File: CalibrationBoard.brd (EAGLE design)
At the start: 100 x 80 mm, 113 parts, among them J1 BANANA_CONN, J2 BANANA_CONN, J3 BANANA_CONN, J4 BANANA_CONN, J5 BANANA_CONN, J6 BANANA_CONN, J7 BANANA_CONN, J8 BANANA_CONN, J9 BANANA_CONN, Q1 IRF540, U1 MAX6126AASA25+, U2 MAX6126AASA25+, U3 MAX6126AASA50+

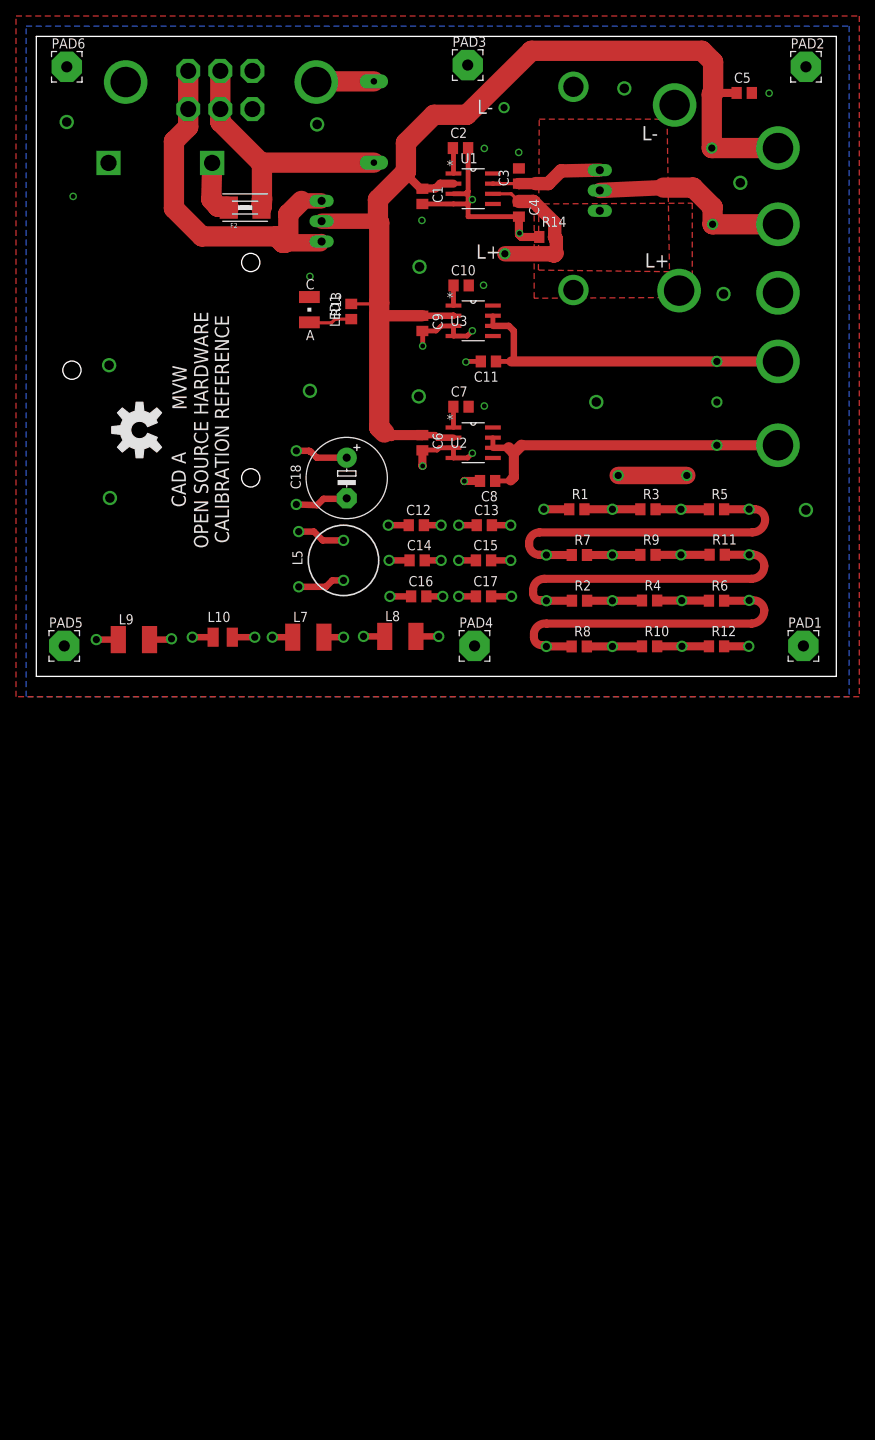
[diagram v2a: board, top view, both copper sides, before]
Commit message: Updates before PCB release to Fabrication
Updates before PCB release to Fabrication.
Component part numbers for purchase still need specifying.
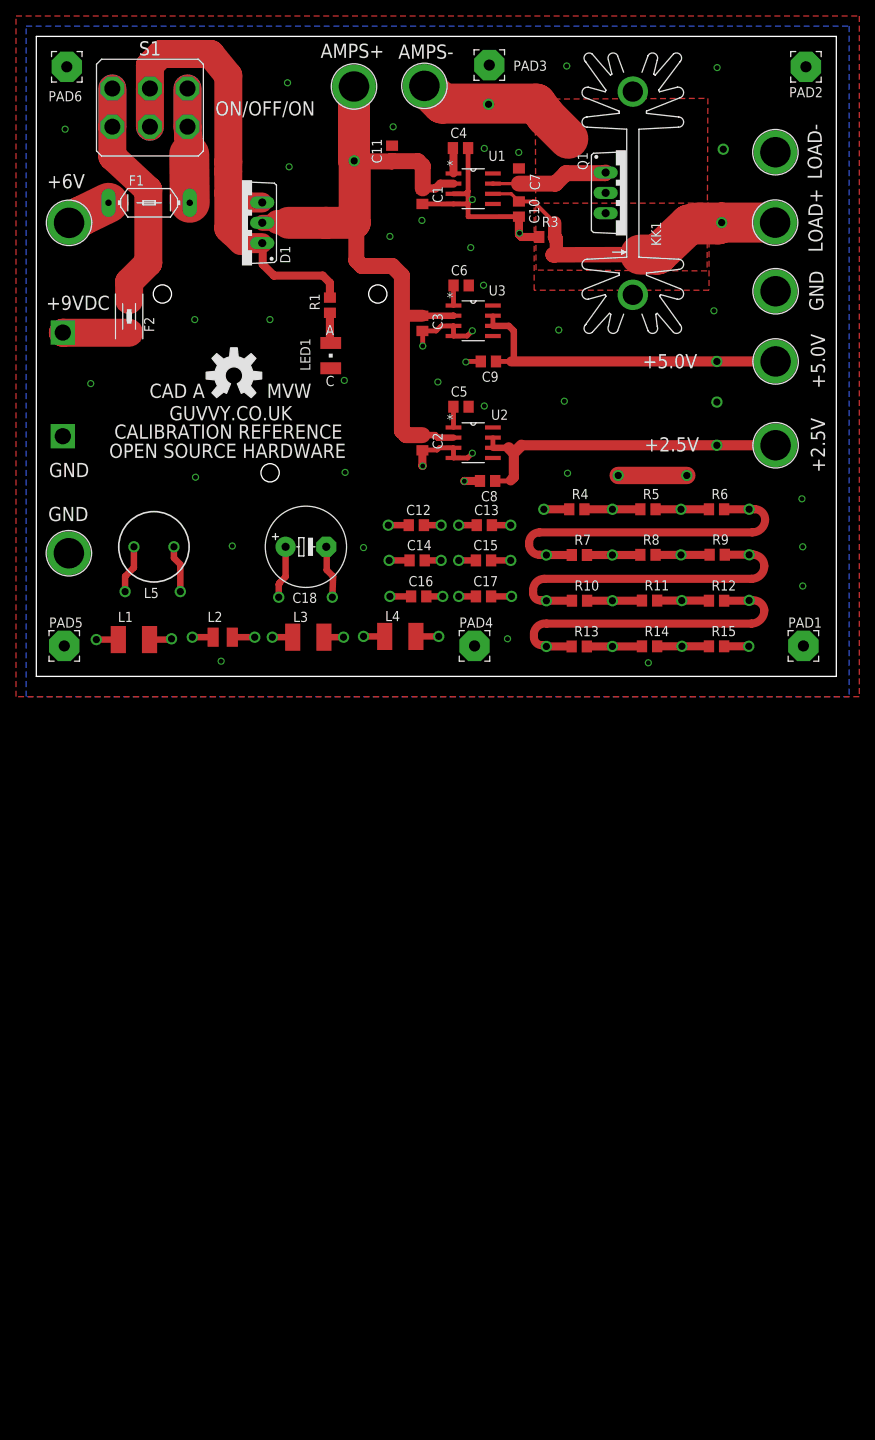
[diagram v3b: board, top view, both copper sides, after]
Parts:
- removed KK2: SK104-PAD, heatsink:SK104-PAD
- removed R2: 1k, rcl:R0805
- removed S3: 6A TOGGLE, switch:320-938
- removed TP51: TP_1MM_TH", TP_1MM_TH:TP_1MM_TH
- added KK1: SK104-PAD, heatsink:SK104-PAD
- added R15: 10Meg, rcl:R0805
- added S1: 5649A, Switch_320-938_Corrected:320-938
- added TP40: TP_1MM_TH", TP_1MM_TH:TP_1MM_TH
- C17: value 100uF -> 10uF
- C18: value (none) -> 100uF
- C2, C7: value 1uF -> 2.2uF
- C5, C6: value 2.2uF -> 1uF
- D1: value 30A_MIN -> MBR60H100CTG
- R1: value 0.1R -> 2k
- R10: value 1Meg -> 1k
- R11: value 100R -> 5k
- R12: value 10Meg -> 10k
- R13: value 2k -> 100k
- R14: value 5R -> 1Meg
- R3: value 1R -> 5R
- R4: value 5k -> 0.1R
- R5: value 5R -> 1R
- R6: value 10k -> 5R
- R8: value 100k -> 50R
- R9: value 50R -> 100R
- moved TP35 64.0 mm to (80.7, 9.48), flipped to the bottom
- moved J2 59.3 mm to (4.07, 15.4), flipped to the top
- moved TP39 58.1 mm to (89.1, 3.76), flipped to the bottom
- moved BAT1 56.7 mm to (56.4, 21.6), turned to 0 degrees
- moved C5 52.8 mm to (53.1, 33.7)
- moved R14 52.8 mm to (76.7, 3.76)
- moved TP4 52.6 mm to (56.5, 71.5), flipped to the top
- moved TP21 52.4 mm to (37.0, 9.90), flipped to the top, turned to 90 degrees
- moved TP3 51.3 mm to (39.7, 64.4), flipped to the top
- moved R13 50.6 mm to (67.9, 3.75), turned to 0 degrees
- moved J5 48.0 mm to (39.7, 73.7), flipped to the top
- moved TP12 46.2 mm to (44.2, 10.0), turned to 0 degrees
- moved TP10 45.5 mm to (44.1, 14.5), flipped to the top
- moved TP28 45.4 mm to (63.8, 15.2), flipped to the bottom
- moved TP7 45.4 mm to (85.1, 34.3), flipped to the top
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- renumbered L10 to L2, L7 to L3, L8 to L4, L9 to L1
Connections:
- removed net N$2: D1.A1, D1.A2, S3.3, S3.6
- removed net N$4: LED1.A, R13.1
- removed net Q1_DRAIN: J4.P$1, Q1.D, TP2.P$1
- removed net VIN_1: F1.2, F2.2, S3.2, S3.5
- removed net V_IN2: C1.1, C5.1, C6.1, C9.1, D1.C, J3.P$1, R13.2, TP1.P$1, U1.2, U2.2, U3.2
- new net I_METER-: J6.P$1, Q1.D, TP4.P$1
- new net N$30: LED1.A, R1.1
- new net V_IN_1: D1.A1, D1.A2, R1.2, S1.2, S1.5
- new net V_IN_2: C1.1, C11.1, C2.1, C3.1, D1.C, J5.P$1, TP3.P$1, U1.2, U2.2, U3.2
- new net V_IN_A: F1.2, S1.3, S1.6
- new net V_IN_B: F2.2, S1.1, S1.4
- net +2.5V_REF: now also J3.P$1, TP5.P$1; no longer J7.P$1, TP9.P$1
- net +5.0V_REF: now also C9.1, J4.P$1, TP6.P$1; no longer C11.1, J9.P$1, TP11.P$1
- net GND: now also J9.P$1, KK1.K1, KK1.K2, R3.1, TP2.P$1; no longer J6.P$1, KK2.K1, KK2.K2, R14.1, TP10.P$1
- net N$1: now also TP8.P$1; no longer TP26.P$1
- net N$10: now also R4.2, R5.1, TP26.P$1; no longer R1.2, R3.1, TP8.P$1
- net N$11: now also TP20.P$1; no longer TP30.P$1
- net N$12: now also R10.1, R9.2, TP25.P$1, TP31.P$1; no longer R11.2, R2.1, TP15.P$1, TP24.P$1
- net N$13: now also R10.2, R11.1, TP34.P$1; no longer R2.2, R4.1, TP16.P$1
- net N$14: now also TP47.P$1; no longer TP37.P$1
- net N$15: now also C5.1; no longer C7.1
- net N$16: now also R11.2, R12.1, TP35.P$1; no longer R4.2, R6.1, TP17.P$1
- net N$17: now also R13.2, R14.1, TP37.P$1; no longer R10.1, R8.2, TP19.P$1
- net N$18: now also R6.2, TP24.P$1, TP28.P$1; no longer R5.2, TP12.P$1, TP13.P$1
- net N$19: now also TP48.P$1; no longer TP38.P$1
- net N$20: now also TP49.P$1; no longer TP39.P$1
- net N$21: now also R14.2, R15.1, TP38.P$1; no longer R10.2, R12.1, TP20.P$1
- net N$22: now also TP22.P$1, TP33.P$1; no longer TP3.P$1, TP4.P$1
- net N$23: now also TP40.P$1; no longer TP42.P$1
- net N$24: now also R15.2, TP39.P$1; no longer R12.2, TP21.P$1
- net N$25: now also TP14.P$1; no longer TP41.P$1
- net N$26: now also TP21.P$1; no longer TP51.P$1
- net N$28: now also C4.1; no longer C2.1
- net N$29: now also R8.1, TP29.P$1; no longer R9.1, TP14.P$1
- net N$3: now also TP45.P$1; no longer TP35.P$1
- net N$31: now also R5.2, R6.1, TP27.P$1; no longer R3.2, R5.1, TP23.P$1
- net N$34: now also R12.2, R13.1, TP32.P$1, TP36.P$1; no longer R6.2, R8.1, TP18.P$1, TP25.P$1
- net N$48: now also TP15.P$1; no longer TP27.P$1
- net N$49: now also TP16.P$1; no longer TP32.P$1
- net N$5: now also R4.1, TP23.P$1; no longer R1.1, TP5.P$1
- net N$50: now also TP17.P$1; no longer TP33.P$1
- net N$51: now also TP18.P$1; no longer TP29.P$1
- net N$52: now also TP19.P$1; no longer TP31.P$1
- net N$53: now also TP9.P$1; no longer TP34.P$1
- net N$54: now also TP10.P$1; no longer TP44.P$1
- net N$55: now also TP11.P$1; no longer TP46.P$1
- net N$56: now also TP12.P$1; no longer TP47.P$1
- net N$57: now also TP13.P$1; no longer TP48.P$1
- net N$59: now also TP44.P$1; no longer TP43.P$1
- net N$6: now also C6.1; no longer C10.1
- net N$60: now also TP43.P$1; no longer TP49.P$1
- net N$61: now also TP42.P$1; no longer TP45.P$1
- net N$62: now also TP41.P$1; no longer TP28.P$1
- net N$7: now also TP46.P$1; no longer TP36.P$1
- net N$8: now also R8.2, R9.1, TP30.P$1; no longer R11.1, R9.2, TP22.P$1
- net OUTF: now also C7.1; no longer C3.1
- net OUTS: now also C10.1, J7.P$1, R3.2, TP1.P$1; no longer C4.1, J5.P$1, R14.2, TP6.P$1
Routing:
- net V_IN2: track 140.2 -> 0.00 mm
- net V_IN_2: track 0.00 -> 89.0 mm
- net V_IN_1: track 0.00 -> 72.6 mm
- net N$2: track 46.8 -> 0.00 mm
- net VIN_1: track 34.4 -> 0.00 mm
- net V_IN_B: track 0.00 -> 34.2 mm
- net I_METER-: track 0.00 -> 29.8 mm
- net OUTS: track 19.7 -> 46.1 mm
- net Q1_DRAIN: track 25.4 -> 0.00 mm
- net V_IN_A: track 0.00 -> 19.1 mm
- net N$4: track 5.45 -> 0.00 mm
- net N$30: track 0.00 -> 3.81 mm
- net +6V_IN: track 7.24 -> 5.53 mm
- net N$9: track 7.18 -> 8.30 mm
- net OUTF: track 14.0 -> 14.7 mm
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- added copper zone on layer 1, net I_METER-
- removed copper zone on layer 1, net Q1_DRAIN
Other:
- board text added: "+6V"
- board text added: "+9VDC"
- board text added: "-=BATTERY HOLDER THIS SIDE=-"
- board text added: "AMPS+"
- board text added: "AMPS-"
- board text added: "GUVVY.CO.UK"
- board text added: "ON/OFF/ON"
- board text removed: "(+6V)"
- board text removed: "(0V)"
- board text removed: "AMP+"
- board text removed: "AMP-"
- board text removed: "L+"
- board text removed: "L-"
